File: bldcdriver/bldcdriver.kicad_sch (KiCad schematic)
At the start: 16 parts, among them Q1 IRF3205, Q2 IRF3205, Q3 IRF3205, Q4 IRF3205, Q5 IRF3205, Q6 IRF3205, U1 DRV8304HRHAR, U2 RP2040

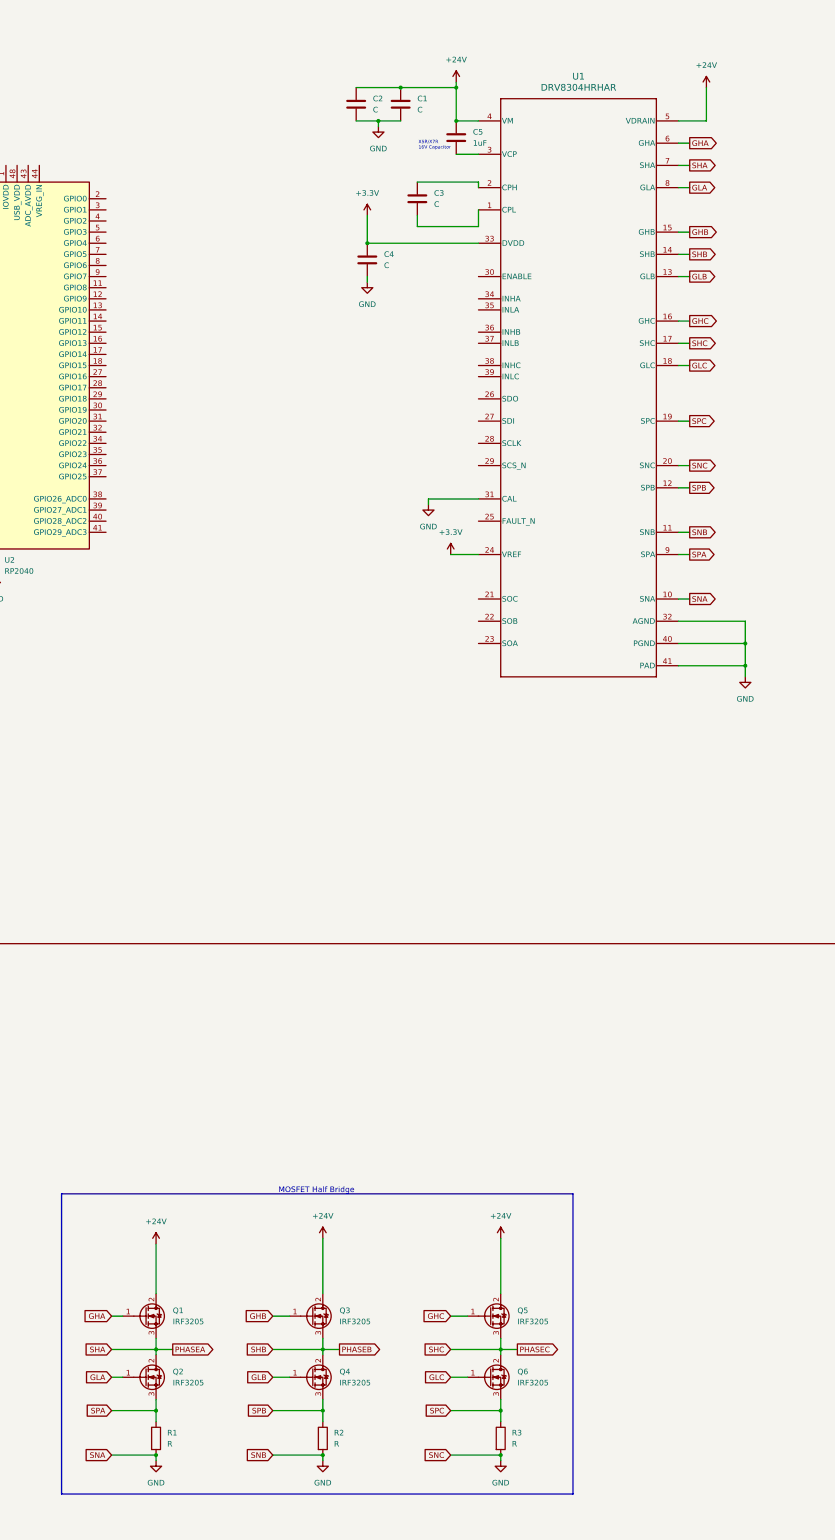
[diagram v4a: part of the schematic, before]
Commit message: Replaced the mistake in symbol from H to S, redid the connections, cleaned up local library folders, added proper net labels
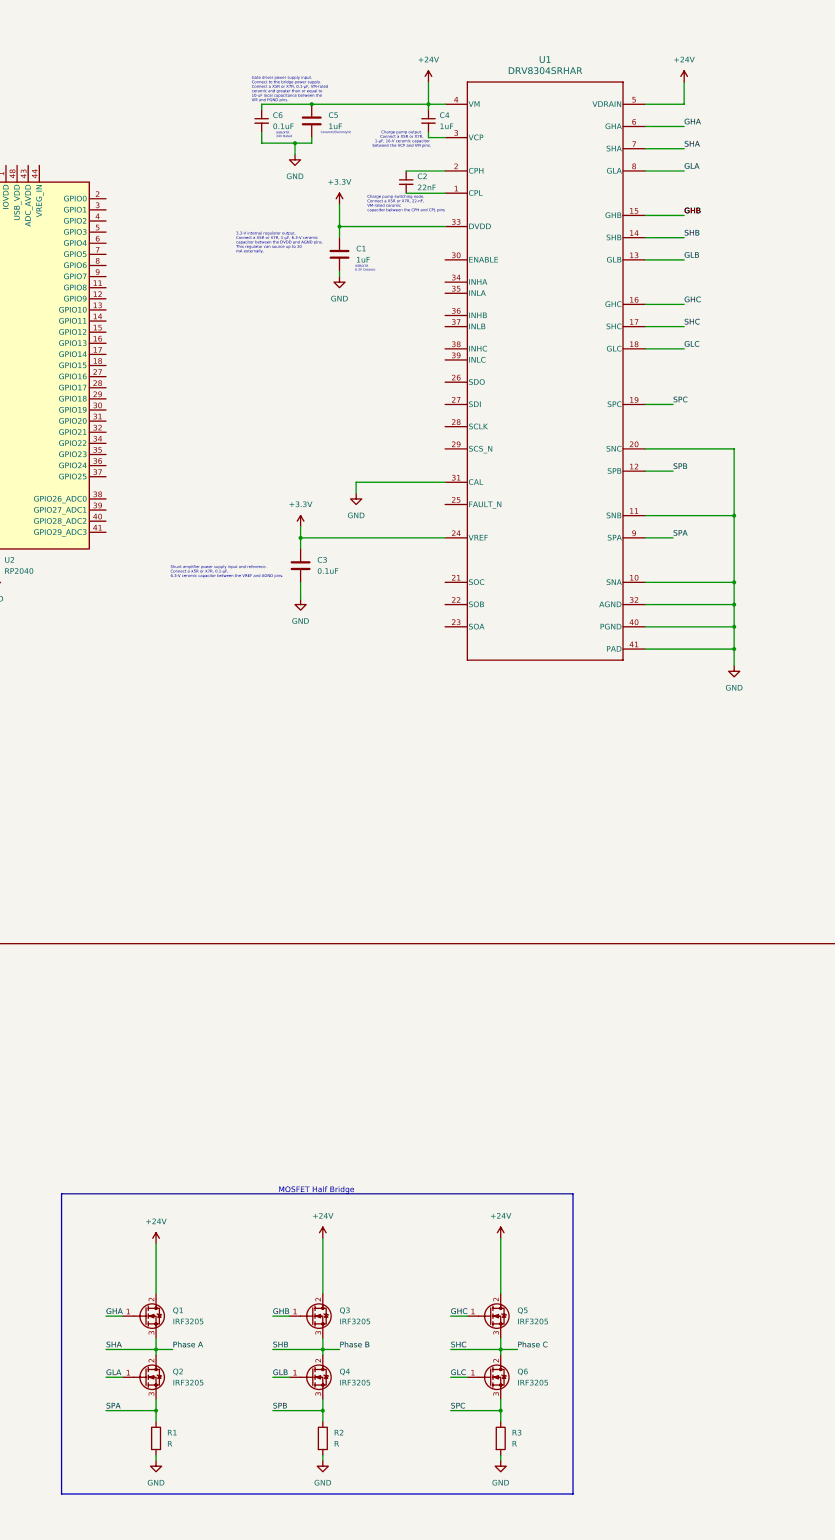
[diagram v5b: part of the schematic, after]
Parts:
- removed C2, C4: C, symbol Device:C
- removed U1: DRV8304HRHAR, DRV8304:RHA0040E, symbol DRV8304:DRV8304HRHAR
- added C2: 22nF, symbol Device:C_Small
- added C4: 1uF, symbol Device:C_Small
- added C6: 0.1uF, symbol Device:C_Small
- added U1: DRV8304SRHAR, RHA0040E, symbol DRV8304S:DRV8304SRHAR
- C1: value C -> 1uF
- C3: value C -> 0.1uF
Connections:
- net +24V: now also C4.1, C6.1, U1.4 (VM), U1.5 (VDRAIN); no longer C1.1
- net +3.3V: now also C1.1, C3.1, U1.24 (VREF), U1.33 (DVDD)
- net GHA: now also U1.6 (GHA)
- net GHB: now also U1.15 (GHB)
- net GHC: now also U1.16 (GHC)
- net GLA: now also U1.8 (GLA)
- net GLB: now also U1.13 (GLB)
- net GLC: now also U1.18 (GLC)
- net GND: now also C3.2, C5.2, C6.2, U1.10 (SNA), U1.11 (SNB), U1.20 (SNC), U1.31 (CAL), U1.32 (AGND), U1.40 (PGND), U1.41 (PAD)
- net SPA: now also U1.9 (SPA)
- net SPB: now also U1.12 (SPB)
- net SPC: now also U1.19 (SPC)
- net PHASEA renamed Phase A
- net Phase A: now also U1.7 (SHA)
- net PHASEB renamed Phase B
- net Phase B: now also U1.14 (SHB)
- net PHASEC renamed Phase C
- net Phase C: now also U1.17 (SHC)
- new net: C4.2, U1.3 (VCP)
- new net: C2.1, U1.2 (CPH)
- new net: C2.2, U1.1 (CPL)
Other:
- note added: "3.3-V internal regulator output. Connect a X5R or X7R, 1-μF, 6.3-V ceramic capacitor between the DVDD and AGND pins. This regulator can source up to 30 mA externally."
- note added: "Ceramic/Electrolytic"
- note added: "Charge pump output. Connect a X5R or X7R, 1-μF, 16-V ceramic capacitor between the VCP and VM pins."
- note added: "Charge pump switching node. Connect a X5R or X7R, 22-nF, VM-rated ceramic capacitor between the CPH and CPL pins"
- note added: "Gate driver power supply input. Connect to the bridge power supply. Connect a X5R or X7R, 0.1-μF, VM-rated ceramic and greater than or equal to 10-uF local capacitance between the VM and PGND pins."
- note added: "Shunt amplifier power supply input and reference. Connect a X5R or X7R, 0.1-μF, 6.3-V ceramic capacitor between the VREF and AGND pins."
- note added: "X5R/X7R 24V Rated"
- note added: "X5R/X7R 6.3V Ceramic"
- note removed: "X5R/X7R 16V Capacitor"

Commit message: Created hierarchical sheets for every major component with a very basic block diagram on the front page
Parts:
- removed C1, C5: 1uF, symbol Device:C
- removed C2: 22nF, symbol Device:C_Small
- removed C3: 0.1uF, symbol Device:C
- removed C4: 1uF, symbol Device:C_Small
- removed C6: 0.1uF, symbol Device:C_Small
- removed Q1, Q2, Q3, Q4, Q5, Q6: IRF3205, Package_TO_SOT_THT:TO-220-3_Horizontal_TabDown, symbol Transistor_FET:IRF3205
- removed R1, R2, R3: R, Resistor_SMD:R_0201_0603Metric, symbol Device:R
- removed U1: DRV8304SRHAR, RHA0040E, symbol DRV8304S:DRV8304SRHAR
- removed U2: RP2040, Package_DFN_QFN:QFN-56-1EP_7x7mm_P0.4mm_EP3.2x3.2mm, symbol MCU_RaspberryPi:RP2040
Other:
- added sheet DRV Sheet (drv_bldc.kicad_sch)
- added sheet rp2040_sheet (rp2040_bldc.kicad_sch)
- note removed: "3.3-V internal regulator output. Connect a X5R or X7R, 1-μF, 6.3-V ceramic capacitor between the DVDD and AGND pins. This regulator can source up to 30 mA externally."
- note removed: "Ceramic/Electrolytic"
- note removed: "Charge pump output. Connect a X5R or X7R, 1-μF, 16-V ceramic capacitor between the VCP and VM pins."
- note removed: "Charge pump switching node. Connect a X5R or X7R, 22-nF, VM-rated ceramic capacitor between the CPH and CPL pins"
- note removed: "Gate driver power supply input. Connect to the bridge power supply. Connect a X5R or X7R, 0.1-μF, VM-rated ceramic and greater than or equal to 10-uF local capacitance between the VM and PGND pins."
- note removed: "MOSFET Half Bridge"
- note removed: "Shunt amplifier power supply input and reference. Connect a X5R or X7R, 0.1-μF, 6.3-V ceramic capacitor between the VREF and AGND pins."
- note removed: "X5R/X7R 24V Rated"
- note removed: "X5R/X7R 6.3V Ceramic"

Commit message: Increased main sheet size to A2 and fit everything there
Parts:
- added C1: 0.1uF, symbol Device:C_Small
- added C10, C11: 100n, symbol Device:C
- added C12, C20: 1u, symbol Device:C
- added C13, C14, C15, C16, C17, C18, C19, C7: 100n, symbol Device:C_Small
- added C2: 0.1uF, symbol Device:C
- added C3, C4: 1uF, symbol Device:C
- added C5: 22nF, symbol Device:C_Small
- added C6: 1uF, symbol Device:C_Small
- added C8, C9: C_Small, symbol Device:C_Small
- added D1: BAT54W, Package_TO_SOT_SMD:SOT-323_SC-70, symbol Diode:BAT54W
- added J1: USB_C_Receptacle_USB2.0_14P, symbol Connector:USB_C_Receptacle_USB2.0_14P
- added J2, J3: Conn_01x03_Pin, symbol Connector:Conn_01x03_Pin
- added J4: SWD Pins, symbol Connector:Conn_01x04_Pin
- added J5: Conn_01x08_Pin, symbol Connector:Conn_01x08_Pin
- added J6: Conn_01x06_Pin, symbol Connector:Conn_01x06_Pin
- added Q1, Q2, Q3, Q4, Q5, Q6: IRF3205, Package_TO_SOT_THT:TO-220-3_Horizontal_TabDown, symbol Transistor_FET:IRF3205
- added R1, R2, R3: R, Resistor_SMD:R_0201_0603Metric, symbol Device:R
- added R10, R6, R7, R8, R9: R, symbol Device:R_Small
- added R4, R5: 5.1k, symbol Device:R
- added SW1, SW2: SW_Push, Button_Switch_THT:SW_PUSH_6mm, symbol Switch:SW_Push
- added U1: DRV8304SRHAR, RHA0040E, symbol DRV8304S:DRV8304SRHAR
- added U2: W25Q128JVS, Package_SO:SOIC-8_5.23x5.23mm_P1.27mm, symbol Memory_Flash:W25Q128JVS
- added U3: RP2040, RP2040:RP2040-QFN-56, symbol RP2040:RP2040
- added Y1: ABM8-272-T3, symbol Device:Crystal_GND24_Small
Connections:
- new net: C8.2, U3.20 (XIN), Y1.3
- new net: J2.1 (Pin_1), U1.21 (SOC)
- new net: J2.2 (Pin_2), U1.22 (SOB)
- new net: J2.3 (Pin_3), U1.23 (SOA)
- new net: J1.B5 (CC2), R4.1
- new net: J5.8 (Pin_8), U3.11 (GPIO8)
- new net: J5.7 (Pin_7), U3.12 (GPIO9)
- new net: J5.6 (Pin_6), U3.13 (GPIO10)
- new net: J5.5 (Pin_5), U3.14 (GPIO11)
- new net: J5.4 (Pin_4), U3.15 (GPIO12)
- new net: J5.3 (Pin_3), U3.16 (GPIO13)
- new net: J5.2 (Pin_2), U3.17 (GPIO14)
- new net: J5.1 (Pin_1), U3.18 (GPIO15)
- new net: C9.2, U3.21 (XOUT), Y1.1
- new net: J4.2 (Pin_2), U3.24 (SWCLK)
- new net: J4.3 (Pin_3), U3.25 (SWD)
- new net: J4.1 (Pin_1), SW2.2, U3.26 (RUN)
- new net: J6.6 (Pin_6), U3.31 (GPIO20)
- new net: J6.5 (Pin_5), U3.32 (GPIO21)
- new net: J6.4 (Pin_4), U3.34 (GPIO22)
- new net: J6.3 (Pin_3), U3.35 (GPIO23)
- new net: J6.2 (Pin_2), U3.36 (GPIO24)
- new net: J6.1 (Pin_1), U3.37 (GPIO25)
- new net: R10.2, U3.46 (USB_DM)
- new net: R9.1, U3.47 (USB_DP)
- new net: R6.2, SW1.1
- new net: C6.2, U1.3 (VCP)
- new net: C5.1, U1.2 (CPH)
- new net: C5.2, U1.1 (CPL)
- new net: J1.A5 (CC1), R5.1
- new net +1V1: C10.1, C11.1, C12.1, U3.23 (DVDD), U3.45 (VREG_VOUT), U3.50 (DVDD)
- new net +24V: C1.1, C3.1, C6.1, Q1.2 (D), Q3.2 (D), Q5.2 (D), U1.4 (VM), U1.5 (VDRAIN)
- new net +3.3V: C13.1, C14.1, C15.1, C16.1, C17.1, C18.1, C19.1, C2.1, C20.1, C4.1, C7.1, R7.1, R8.2, U1.24 (VREF), U1.33 (DVDD), U2.8 (VCC), U3.1 (IOVDD), U3.10 (IOVDD), U3.22 (IOVDD), U3.33 (IOVDD), U3.42 (IOVDD), U3.43 (ADC_AVDD), U3.44 (VREG_IN), U3.48 (USB_VDD), U3.49 (IOVDD)
- new net +5V: D1.3 (K)
- new net D+: J1.A6 (D+), J1.B6 (D+), R9.2
- new net D-: J1.A7 (D-), J1.B7 (D-), R10.1
- new net DREN: U1.30 (ENABLE), U3.8 (GPIO6)
- new net GHA: Q1.1 (G), U1.6 (GHA)
- new net GHB: Q3.1 (G), U1.15 (GHB)
- new net GHC: Q5.1 (G), U1.16 (GHC)
- new net GLA: Q2.1 (G), U1.8 (GLA)
- new net GLB: Q4.1 (G), U1.13 (GLB)
- new net GLC: Q6.1 (G), U1.18 (GLC)
- new net GND: C1.2, C10.2, C11.2, C12.2, C13.2, C14.2, C15.2, C16.2, C17.2, C18.2, C19.2, C2.2, C20.2, C3.2, C4.2, C7.2, C8.1, C9.1, J1.A1 (GND), J1.A12 (GND), J1.B1 (GND), J1.B12 (GND), J1.S1 (SHIELD), J4.4 (Pin_4), R1.2, R2.2, R3.2, R4.2, R5.2, SW1.2, SW2.1, U1.10 (SNA), U1.11 (SNB), U1.20 (SNC), U1.31 (CAL), U1.32 (AGND), U1.40 (PGND), U1.41 (PAD), U2.4 (GND), U3.19 (TESTEN), U3.57 (GND)
- new net INHA: U1.34 (INHA), U3.2 (GPIO0)
- new net INHB: U1.36 (INHB), U3.4 (GPIO2)
- new net INHC: U1.38 (INHC), U3.6 (GPIO4)
- new net INLA: U1.35 (INLA), U3.3 (GPIO1)
- new net INLB: U1.37 (INLB), U3.5 (GPIO3)
- new net INLC: U1.39 (INLC), U3.7 (GPIO5)
- new net Phase A: Q1.3 (S), Q2.2 (D), U1.7 (SHA)
- new net Phase B: Q3.3 (S), Q4.2 (D), U1.14 (SHB)
- new net Phase C: Q5.3 (S), Q6.2 (D), U1.17 (SHC)
- new net QSPI_SCLK: U2.6 (CLK), U3.52 (QSPI_SCLK)
- new net QSPI_SD0: U2.5 (DI(IO0)), U3.53 (QSPI_SD0)
- new net QSPI_SD1: U2.2 (DO(IO1)), U3.55 (QSPI_SD1)
- new net QSPI_SD2: U2.3 (IO2), U3.54 (QSPI_SD2)
- new net QSPI_SD3: U2.7 (IO3), U3.51 (QSPI_SD3)
- new net QSPI_SS: R6.1, R7.2, U2.1 (~{CS}), U3.56 (QSPI_SS)
- new net SPA: Q2.3 (S), R1.1, U1.9 (SPA)
- new net SPB: Q4.3 (S), R2.1, U1.12 (SPB)
- new net SPC: Q6.3 (S), R3.1, U1.19 (SPC)
- new net SPI_CLK: J3.3 (Pin_3), U1.28 (SCLK), U3.29 (GPIO18)
- new net SPI_CSn_DRV: U1.29 (SCS_N), U3.28 (GPIO17)
- new net SPI_SDI: J3.1 (Pin_1), U1.26 (SDO), U3.27 (GPIO16)
- new net SPI_SDO: J3.2 (Pin_2), U1.27 (SDI), U3.30 (GPIO19)
- new net VBUS: D1.1 (A), J1.A4 (VBUS), J1.A9 (VBUS), J1.B4 (VBUS), J1.B9 (VBUS)
- new net nFAULT: R8.1, U1.25 (FAULT_N), U3.9 (GPIO7)
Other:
- removed sheet DRV Sheet
- removed sheet Power Sheet
- removed sheet Three Phase Half Bridge
- removed sheet rp2040_sheet
- note added: "3.3-V internal regulator output. Connect a X5R or X7R, 1-μF, 6.3-V ceramic capacitor between the DVDD and AGND pins. This regulator can source up to 30 mA externally."
- note added: "C7 should be close to Pin 45"
- note added: "Ceramic/Electrolytic"
- note added: "Charge pump output. Connect a X5R or X7R, 1-μF, 16-V ceramic capacitor between the VCP and VM pins."
- note added: "Charge pump switching node. Connect a X5R or X7R, 22-nF, VM-rated ceramic capacitor between the CPH and CPL pins"
- note added: "DRV8304S"
- note added: "Gate driver power supply input. Connect to the bridge power supply. Connect a X5R or X7R, 0.1-μF, VM-rated ceramic and greater than or equal to 10-uF local capacitance between the VM and PGND pins."
- note added: "Input"
- note added: "MOSFET Half Bridge"
- note added: "Output"
- note added: "Place near pin 44"
- note added: "Power"
- note added: "RP2040"
- note added: "Shunt amplifier power supply input and reference. Connect a X5R or X7R, 0.1-μF, 6.3-V ceramic capacitor between the VREF and AGND pins."
- note added: "X5R/X7R 24V Rated"
- note added: "X5R/X7R 6.3V Ceramic"
